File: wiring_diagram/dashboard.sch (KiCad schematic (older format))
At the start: 27 parts

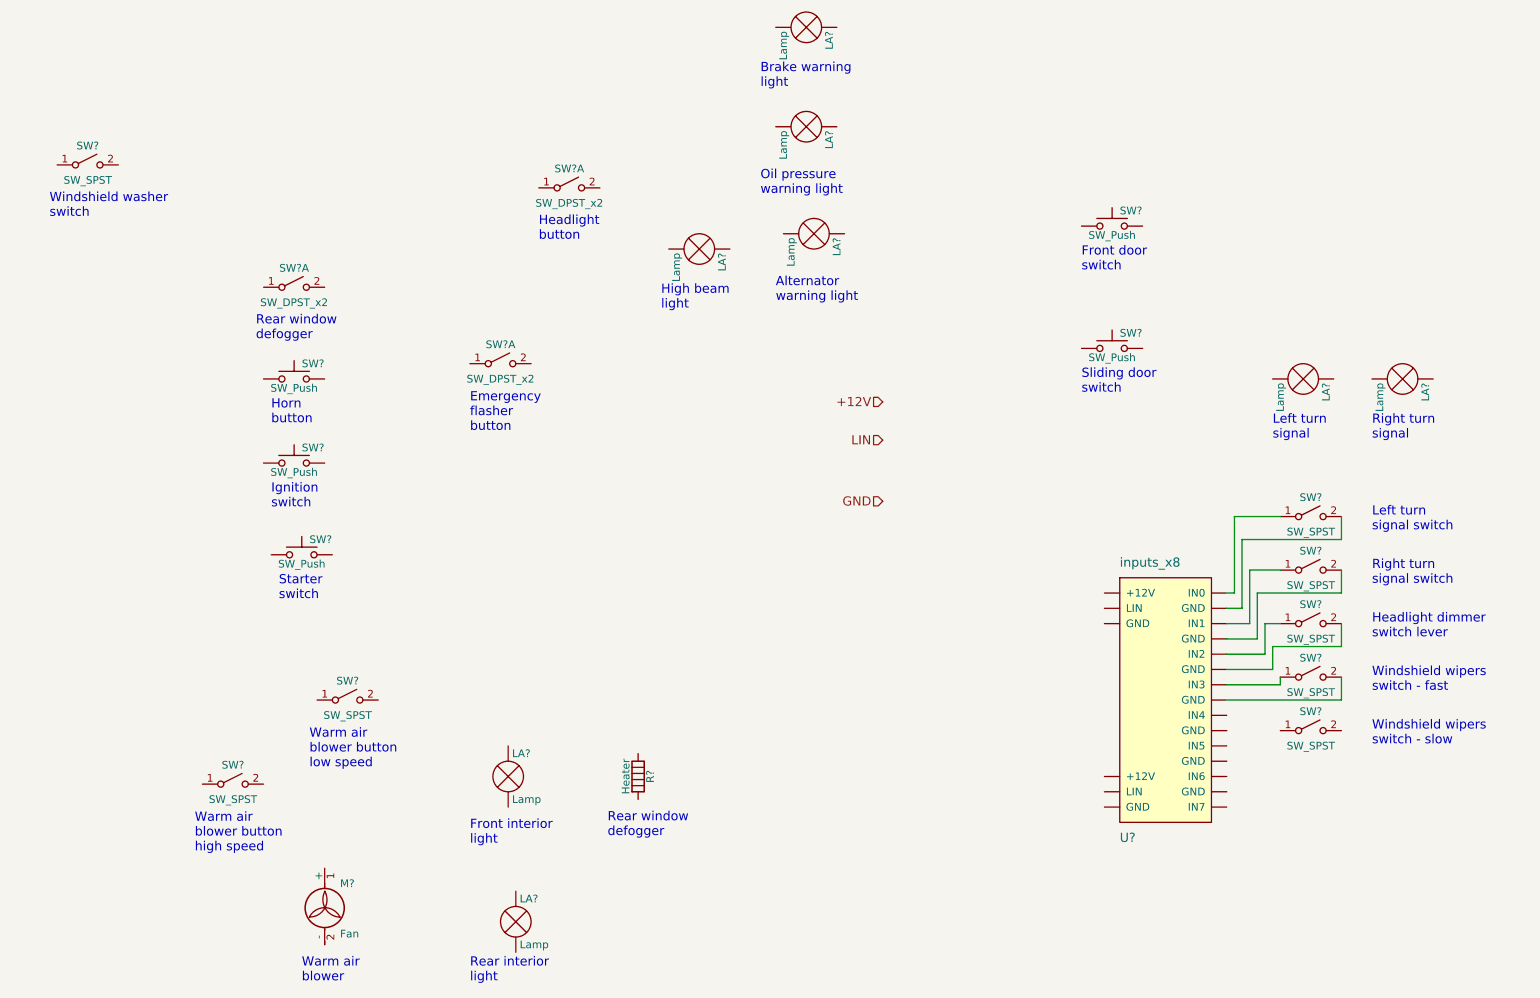
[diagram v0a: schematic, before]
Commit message: updated wiring diagram
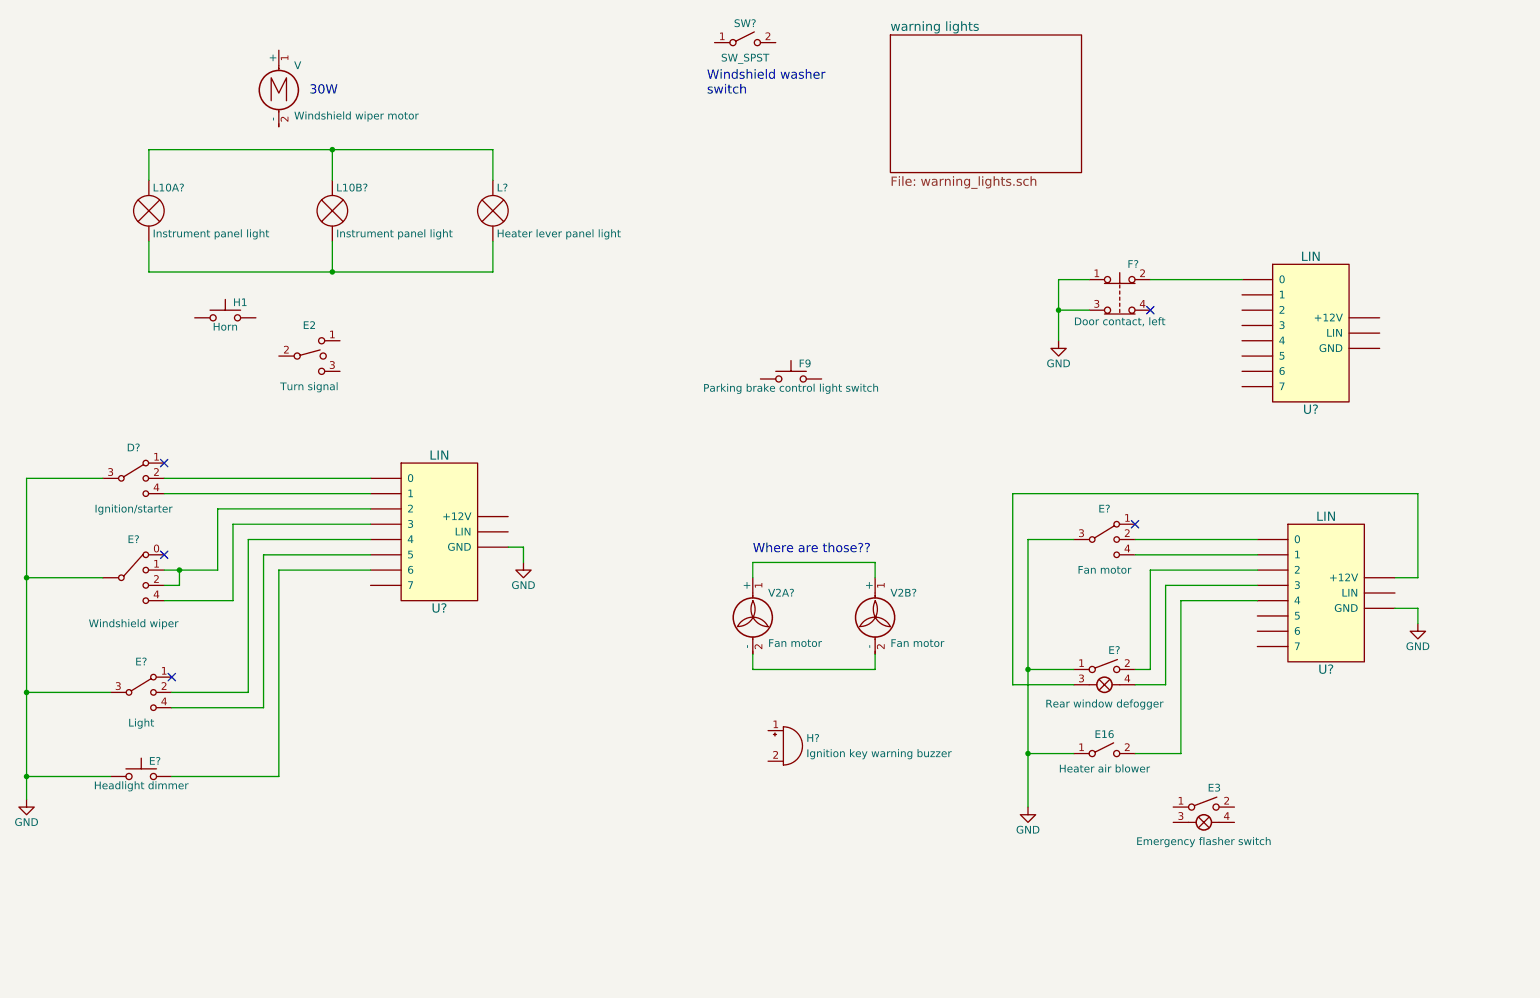
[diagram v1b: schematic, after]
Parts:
- removed LA? (x8): Lamp, symbol Lamp
- removed M?: Fan, symbol Fan
- removed R?: Heater, symbol Heater
- removed SW? (x5): SW_Push, symbol SW_Push
- removed SW? (x3): SW_DPST_x2, symbol SW_DPST_x2
- removed SW? (x8): SW_SPST, symbol SW_SPST
- removed U?: inputs_x8, symbol inputs_x8
- added D?: Ignition/starter, symbol SW_SP3T
- added E16: Heater air blower, symbol SW_SPST
- added E2: Turn signal, symbol SW_SPDT_MSM
- added E3: Emergency flasher switch, symbol SW_SPST_Lamp
- added E?: Windshield wiper, symbol SW_SP4T
- added E?: Light, symbol SW_SP3T
- added E?: Headlight dimmer, symbol SW_Push
- added E?: Fan motor, symbol SW_SP3T
- added E?: Rear window defogger, symbol SW_SPST_Lamp
- added F9: Parking brake control light switch, symbol SW_Push
- added F?: Door contact, left, symbol SW_Push_Open_Dual
- added H1: Horn, symbol SW_Push
- added H?: Ignition key warning buzzer, symbol Buzzer
- added L10A?, L10B?: Instrument panel light, symbol Lamp
- added L?: Heater lever panel light, symbol Lamp
- added SW?: SW_SPST, symbol SW_SPST
- added U? (x3): LIN, symbol LIN
- added V: Windshield wiper motor, symbol Motor_DC
- added V2A?, V2B?: Fan motor, symbol Fan
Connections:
- net GND: now also D?.3, E16.1 (A), E?.1, E?.1, E?.3, E?.3, E?.~, F?.1, F?.3, U?.~ (LIN), U?.~ (LIN)
- new net: D?.2, U?.~ (LIN)
- new net: D?.4, U?.~ (LIN)
- new net: E?.1, E?.2, U?.~ (LIN)
- new net: E?.4, U?.~ (LIN) (x3)
- new net: E?.2, U?.~ (LIN) (x4)
- new net: L10A?.1 (-), L10B?.1 (-), L?.1 (-)
- new net: L10A?.2 (+), L10B?.2 (+), L?.2 (+)
- new net: E?.3 (L), U?.~ (LIN)
- new net: E?.4 (L), U?.~ (LIN)
- new net: E16.2 (B), U?.~ (LIN)
- new net: F?.2, U?.~ (LIN)
- new net: V2A?.1 (+), V2B?.1 (+)
- new net: V2A?.2 (-), V2B?.2 (-)
- no-connect marks 0 -> 5
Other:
- note added: "30W"
- note added: "Where are those??"
- note removed: "Alternator\nwarning light"
- note removed: "Brake warning\nlight"
- note removed: "Emergency\nflasher\nbutton"
- note removed: "Front door\nswitch"
- note removed: "Front interior\nlight"
- note removed: "Headlight dimmer\nswitch lever"
- note removed: "Headlight\nbutton"
- note removed: "High beam\nlight"
- note removed: "Horn\nbutton"
- note removed: "Ignition\nswitch"
- note removed: "Left turn\nsignal"
- note removed: "Left turn\nsignal switch"
- note removed: "Oil pressure\nwarning light"
- note removed: "Rear interior\nlight"
- note removed: "Rear window\ndefogger"
- note removed: "Right turn\nsignal"
- note removed: "Right turn\nsignal switch"
- note removed: "Sliding door\nswitch"
- note removed: "Starter\nswitch"
- note removed: "Warm air\nblower"
- note removed: "Warm air\nblower button\nhigh speed"
- note removed: "Warm air\nblower button\nlow speed"
- note removed: "Windshield wipers\nswitch - fast"
- note removed: "Windshield wipers\nswitch - slow"

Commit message: wiring diagram update
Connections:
- wire segments 66 -> 73
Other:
- note added: "NOT ON WIRING DIAGRAM??"
- moved on the sheet: E2, E?, H1, SW?
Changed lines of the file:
@@
 L SW_Push H1
 U 1 1 5968925E
-P 2900 2950
-F 0 "H1" H 2950 3050 50  0000 L CNN
-F 1 "Horn" H 2900 2890 50  0000 C CNN
-F 2 "" H 2900 3150 50  0000 C CNN
-F 3 "" H 2900 3150 50  0000 C CNN
-	1    2900 2950
+P 2350 6400
+F 0 "H1" H 2400 6500 50  0000 L CNN
+F 1 "Horn" H 2350 6340 50  0000 C CNN
+F 2 "" H 2350 6600 50  0000 C CNN
+F 3 "" H 2350 6600 50  0000 C CNN
+	1    2350 6400
 	1    0    0    -1
 $EndComp
@@
 L SW_SP3T E?
 U 1 1 59689293
-P 2350 5400
-F 0 "E?" H 2350 5600 50  0000 C CNN
-F 1 "Light" H 2350 5200 50  0000 C CNN
-F 2 "" H 1725 5575 50  0001 C CNN
-F 3 "" H 1725 5575 50  0001 C CNN
-	1    2350 5400
-	1    0    0    -1
-$EndComp
-NoConn ~ 2550 5300
+P 6550 2900
+F 0 "E?" H 6550 3100 50  0000 C CNN
+F 1 "Light" H 6550 2700 50  0000 C CNN
+F 2 "" H 5925 3075 50  0001 C CNN
+F 3 "" H 5925 3075 50  0001 C CNN
+	1    6550 2900
+	1    0    0    -1
+$EndComp
+NoConn ~ 6750 2800
 $Comp
 L SW_Push E?
@@
 L GND #PWR?
 U 1 1 596892A2
-P 1600 6100
-F 0 "#PWR?" H 1600 5850 50  0001 C CNN
-F 1 "GND" H 1600 5950 50  0000 C CNN
-F 2 "" H 1600 6100 50  0001 C CNN
-F 3 "" H 1600 6100 50  0001 C CNN
-	1    1600 6100
+P 1600 6600
+F 0 "#PWR?" H 1600 6350 50  0001 C CNN
+F 1 "GND" H 1600 6450 50  0000 C CNN
+F 2 "" H 1600 6600 50  0001 C CNN
+F 3 "" H 1600 6600 50  0001 C CNN
+	1    1600 6600
 	1    0    0    -1
 $EndComp
@@
 	2950 4800 2500 4800
 Wire Wire Line
-	2550 5400 3050 5400
-Wire Wire Line
-	3050 5400 3050 4400
+	6750 2900 7250 2900
+Wire Wire Line
+	3050 5300 3050 4400
 Wire Wire Line
 	3050 4400 3850 4400
@@
 	3150 4500 3150 5500
 Wire Wire Line
-	3150 5500 2550 5500
-Wire Wire Line
-	1600 5400 2150 5400
+	7350 3000 6750 3000
+Wire Wire Line
+	5800 2900 6350 2900
 Wire Wire Line
 	2550 5950 3250 5950
@@
 	1600 5950 2150 5950
 Wire Wire Line
-	1600 4000 1600 6100
+	1600 4000 1600 6600
 Wire Wire Line
 	2400 2050 2400 1850
@@
 L SW_SPDT_MSM E2
 U 1 1 596892E5
-P 3450 3200
-F 0 "E2" H 3450 3400 50  0000 C CNN
-F 1 "Turn signal" H 3450 3000 50  0000 C CNN
-F 2 "" H 3450 3200 50  0001 C CNN
-F 3 "" H 3450 3200 50  0001 C CNN
-	1    3450 3200
-	1    0    0    -1
-$EndComp
-Text Notes 6050 1500 0    60   ~ 0
+P 2350 5400
+F 0 "E2" H 2350 5600 50  0000 C CNN
+F 1 "Turn signal" H 2350 5200 50  0000 C CNN
+F 2 "" H 2350 5400 50  0001 C CNN
+F 3 "" H 2350 5400 50  0001 C CNN
+	1    2350 5400
+	1    0    0    -1
+$EndComp
+Text Notes 3900 5700 0    60   ~ 0
 Windshield washer\nswitch
 $Comp
 L SW_SPST SW?
 U 1 1 5968C2B8
-P 6300 1150
-F 0 "SW?" H 6300 1275 50  0000 C CNN
-F 1 "SW_SPST" H 6300 1050 50  0000 C CNN
-F 2 "" H 6300 1150 50  0000 C CNN
-F 3 "" H 6300 1150 50  0000 C CNN
-	1    6300 1150
+P 4200 5350
+F 0 "SW?" H 4200 5475 50  0000 C CNN
+F 1 "SW_SPST" H 4200 5250 50  0000 C CNN
+F 2 "" H 4200 5350 50  0000 C CNN
+F 3 "" H 4200 5350 50  0000 C CNN
+	1    4200 5350
 	1    0    0    -1
 $EndComp
@@
 	1    0    0    -1
 $EndComp
+Wire Wire Line
+	2150 6400 1600 6400
+Connection ~ 1600 6400
+Wire Wire Line
+	2550 6400 3350 6400
+Wire Wire Line
+	3350 6400 3350 4700
+Wire Wire Line
+	3350 4700 3850 4700
+Wire Wire Line
+	2150 5400 1600 5400
+Wire Wire Line
+	3150 5500 2550 5500
+Wire Wire Line
+	3050 5300 2550 5300
+Text Notes 3800 5900 0    60   ~ 0
+NOT ON WIRING DIAGRAM??
 $EndSCHEMATC

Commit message: Adding fuel pump driver
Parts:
- D?, E? (x2): symbol SW_SP3T -> wiring_diagram-rescue:SW_SP3T
- E16, SW?: symbol SW_SPST -> wiring_diagram-rescue:SW_SPST
- E2: symbol SW_SPDT_MSM -> wiring_diagram-rescue:SW_SPDT_MSM
- E3, E?: symbol SW_SPST_Lamp -> wiring_diagram-rescue:SW_SPST_Lamp
- E?: symbol SW_SP4T -> sw_sp4t:SW_SP4T
- E?, F9, H1: symbol SW_Push -> wiring_diagram-rescue:SW_Push
- F?: symbol SW_Push_Open_Dual -> wiring_diagram-rescue:SW_Push_Open_Dual
- H?: symbol Buzzer -> wiring_diagram-rescue:Buzzer
- L10A?, L10B?, L?: symbol Lamp -> wiring_diagram-rescue:Lamp
- U? (x3): symbol LIN -> lin:LIN
- V: symbol Motor_DC -> wiring_diagram-rescue:Motor_DC
- V2A?, V2B?: symbol Fan -> wiring_diagram-rescue:Fan
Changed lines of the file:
@@
-EESchema Schematic File Version 2
-LIBS:power
-LIBS:device
-LIBS:transistors
-LIBS:conn
-LIBS:linear
-LIBS:regul
-LIBS:74xx
-LIBS:cmos4000
-LIBS:adc-dac
-LIBS:memory
-LIBS:xilinx
-LIBS:microcontrollers
-LIBS:dsp
-LIBS:microchip
-LIBS:analog_switches
-LIBS:motorola
-LIBS:texas
-LIBS:intel
-LIBS:audio
-LIBS:interface
-LIBS:digital-audio
-LIBS:philips
-LIBS:display
-LIBS:cypress
-LIBS:siliconi
-LIBS:opto
-LIBS:atmel
-LIBS:contrib
-LIBS:valves
-LIBS:13a_switch_x4
-LIBS:switches
-LIBS:motors
-LIBS:inputs_x8
-LIBS:lin
-LIBS:sw_sp4t
-LIBS:tdc_marker_unit
+EESchema Schematic File Version 4
 LIBS:wiring_diagram-cache
-EELAYER 25 0
+EELAYER 26 0
 EELAYER END
 $Descr A4 11693 8268
@@
 $EndDescr
 $Comp
-L SW_Push H1
+L wiring_diagram-rescue:SW_Push H1
 U 1 1 5968925E
 P 2350 6400
@@
 $EndComp
 $Comp
-L Motor_DC V
+L wiring_diagram-rescue:Motor_DC V
 U 1 1 5968926C
 P 3250 1400
@@
 30W
 $Comp
-L LIN U?
+L lin:LIN U?
 U 1 1 59689274
 P 4300 4350
@@
 $EndComp
 $Comp
-L GND #PWR?
+L power:GND #PWR?
 U 1 1 5968927B
 P 4850 4550
@@
 $EndComp
 $Comp
-L SW_SP3T D?
+L wiring_diagram-rescue:SW_SP3T D?
 U 1 1 59689281
 P 2300 4000
@@
 NoConn ~ 2500 3900
 $Comp
-L SW_SP4T E?
+L sw_sp4t:SW_SP4T E?
 U 1 1 5968928B
 P 2300 4650
@@
 NoConn ~ 2500 4500
 $Comp
-L SW_SP3T E?
+L wiring_diagram-rescue:SW_SP3T E?
 U 1 1 59689293
 P 6550 2900
@@
 NoConn ~ 6750 2800
 $Comp
-L SW_Push E?
+L wiring_diagram-rescue:SW_Push E?
 U 1 1 5968929B
 P 2350 5950
@@
 $EndComp
 $Comp
-L GND #PWR?
+L power:GND #PWR?
 U 1 1 596892A2
 P 1600 6600
@@
 $EndComp
 $Comp
-L Lamp L10A?
+L wiring_diagram-rescue:Lamp L10A?
 U 1 1 596892A8
 P 2400 2250
@@
 $EndComp
 $Comp
-L Lamp L10B?
+L wiring_diagram-rescue:Lamp L10B?
 U 1 1 596892AF
 P 3600 2250
@@
 $EndComp
 $Comp
-L Lamp L?
+L wiring_diagram-rescue:Lamp L?
 U 1 1 596892B6
 P 4650 2250
@@
 Connection ~ 1600 4650
 $Comp
-L SW_SPDT_MSM E2
+L wiring_diagram-rescue:SW_SPDT_MSM E2
 U 1 1 596892E5
 P 2350 5400
@@
 Windshield washer\nswitch
 $Comp
-L SW_SPST SW?
+L wiring_diagram-rescue:SW_SPST SW?
 U 1 1 5968C2B8
 P 4200 5350
@@
 $EndComp
 $Comp
-L SW_SP3T E?
+L wiring_diagram-rescue:SW_SP3T E?
 U 1 1 5968C2CF
 P 8650 4400
@@
 $EndComp
 $Comp
-L GND #PWR?
+L power:GND #PWR?
 U 1 1 5968C2D6
 P 8150 6150
@@
 NoConn ~ 8850 4300
 $Comp
-L LIN U?
+L lin:LIN U?
 U 1 1 5968C2DD
 P 10100 4750
@@
 $EndComp
 $Comp
-L GND #PWR?
+L power:GND #PWR?
 U 1 1 5968C2E4
 P 10700 4950
@@
 $EndComp
 $Comp
-L SW_Push_Open_Dual F?
+L wiring_diagram-rescue:SW_Push_Open_Dual F?
 U 1 1 5968C2EA
 P 8750 2700
@@
 $EndComp
 $Comp
-L LIN U?
+L lin:LIN U?
 U 1 1 5968C2F1
 P 10000 3050
@@
 $EndComp
 $Comp
-L GND #PWR?
+L power:GND #PWR?
 U 1 1 5968C2F8
 P 8350 3100
@@
 NoConn ~ 8950 2900
 $Comp
-L Buzzer H?
+L wiring_diagram-rescue:Buzzer H?
 U 1 1 5968C2FF
 P 6550 5750
@@
 $EndComp
 $Comp
-L SW_SPST_Lamp E?
+L wiring_diagram-rescue:SW_SPST_Lamp E?
 U 1 1 5968C306
 P 8650 5350
@@
 	8050 5350 8450 5350
 $Comp
-L SW_SPST E16
+L wiring_diagram-rescue:SW_SPST E16
 U 1 1 5968C325
 P 8650 5800
@@
 Connection ~ 8150 5800
 $Comp
-L Fan V2A?
+L wiring_diagram-rescue:Fan V2A?
 U 1 1 5968C331
 P 6350 4950
@@
 $EndComp
 $Comp
-L Fan V2B?
+L wiring_diagram-rescue:Fan V2B?
 U 1 1 5968C338
 P 7150 4950
@@
 $EndSheet
 $Comp
-L SW_SPST_Lamp E3
+L wiring_diagram-rescue:SW_SPST_Lamp E3
 U 1 1 59683C67
 P 9300 6250
@@
 $EndComp
 $Comp
-L SW_Push F9
+L wiring_diagram-rescue:SW_Push F9
 U 1 1 59684763
 P 6600 3350
